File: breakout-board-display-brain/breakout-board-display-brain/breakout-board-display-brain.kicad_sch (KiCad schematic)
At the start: 8 parts, among them J1 Conn_01x15_Socket, J2 Conn_01x15_Socket, J3 Conn_01x16_Female, SW1 RotaryEncoder_Switch

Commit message: ...
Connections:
- net 0 renamed Pin_0
- net 1 renamed Pin_1
- net 10 renamed Pin_10
- net 18 renamed Pin_18
- net 19 renamed Pin_19
- net 2 renamed Pin_2
- net 3 renamed Pin_3
- net 4 renamed Pin_4
- net 5 renamed Pin_5
- net 6 renamed Pin_6
- net 7 renamed Pin_7
- net 8 renamed Pin_8
- net 9 renamed Pin_9
- no-connect marks 8 -> 14

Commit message: Amir approved: Rotary Encode Circuit
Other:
- note added: "Amir approved"
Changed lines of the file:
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@@
+    (effects (font (size 1.27 1.27)) (justify left bottom))
+  )
+  (text "Amir approved" (at 219.71 53.34 0)
     (effects (font (size 1.27 1.27)) (justify left bottom))
   )

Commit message: Update: nun approved!
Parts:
- removed R1, R2: 10k, symbol Device:R
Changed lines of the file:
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@@
     (comment 1 "erste Version")
   )
-  (junction (at 222.25 31.75) (diameter 0) (color 0 0 0 0)
-  )
   (junction (at 106.68 68.58) (diameter 0) (color 0 0 0 0)
   )
-  (junction (at 237.49 40.64) (diameter 0) (color 0 0 0 0)
-  )
   (junction (at 264.16 44.45) (diameter 0) (color 0 0 0 0)
   )
@@
   )
   (junction (at 106.68 50.8) (diameter 0) (color 0 0 0 0)
-  )
-  (junction (at 234.95 31.75) (diameter 0) (color 0 0 0 0)
   )
   (junction (at 49.53 55.88) (diameter 0) (color 0 0 0 0)
@@
     (stroke (width 0) (type default))
   )
-  (wire (pts (xy 234.95 31.75) (xy 238.76 31.75))
+  (wire (pts (xy 224.79 31.75) (xy 238.76 31.75))
     (stroke (width 0) (type default))
   )
@@
     (stroke (width 0) (type default))
   )
-  (wire (pts (xy 238.76 40.64) (xy 237.49 40.64))
+  (wire (pts (xy 238.76 40.64) (xy 224.79 40.64))
     (stroke (width 0) (type default))
   )
@@
     (stroke (width 0) (type default))
   )
-  (wire (pts (xy 222.25 22.86) (xy 222.25 31.75))
-    (stroke (width 0) (type default))
-  )
   (wire (pts (xy 116.84 49.53) (xy 123.19 49.53))
     (stroke (width 0) (type default))
@@
     (stroke (width 0) (type default))
   )
-  (wire (pts (xy 237.49 40.64) (xy 232.41 40.64))
-    (stroke (width 0) (type default))
-  )
   (wire (pts (xy 92.71 60.96) (xy 99.06 60.96))
     (stroke (width 0) (type default))
@@
     (stroke (width 0) (type default))
   )
-  (wire (pts (xy 222.25 31.75) (xy 222.25 40.64))
-    (stroke (width 0) (type default))
-  )
-  (wire (pts (xy 234.95 31.75) (xy 232.41 31.75))
-    (stroke (width 0) (type default))
-  )
   (wire (pts (xy 190.5 31.75) (xy 203.2 31.75))
     (stroke (width 0) (type default))
@@
     (stroke (width 0) (type default))
   )
-  (wire (pts (xy 237.49 29.21) (xy 237.49 40.64))
+  (wire (pts (xy 224.79 39.37) (xy 224.79 40.64))
     (stroke (width 0) (type default))
   )
@@
     (stroke (width 0) (type default))
   )
-  (wire (pts (xy 222.25 40.64) (xy 224.79 40.64))
-    (stroke (width 0) (type default))
-  )
   (wire (pts (xy 54.61 24.13) (xy 54.61 35.56))
     (stroke (width 0) (type default))
@@
     (stroke (width 0) (type default))
   )
-  (wire (pts (xy 222.25 31.75) (xy 224.79 31.75))
-    (stroke (width 0) (type default))
-  )
   (wire (pts (xy 63.5 40.64) (xy 68.58 40.64))
     (stroke (width 0) (type default))
@@
     (stroke (width 0) (type default))
   )
-  (wire (pts (xy 234.95 22.86) (xy 234.95 31.75))
-    (stroke (width 0) (type default))
-  )
   (polyline (pts (xy 215.9 15.24) (xy 215.9 76.2))
     (stroke (width 0) (type default))
@@
     (stroke (width 0) (type default))
   )
-  (text "CLK\n" (at 234.95 20.32 0)
+  (text "CLK\n" (at 224.79 36.83 0)
     (effects (font (size 1.27 1.27)) (justify left bottom))
   )
@@
     (effects (font (size 1.27 1.27)) (justify left bottom))
   )
-  (text "DT\n" (at 237.49 26.67 0)
+  (text "DT\n" (at 224.79 29.21 0)
     (effects (font (size 1.27 1.27)) (justify left bottom))
   )
@@
     (effects (font (size 1.27 1.27)) (justify left bottom))
   )
-  (label "Pin_4" (at 234.95 22.86 0) (fields_autoplaced)
+  (label "Pin_4" (at 224.79 31.75 0) (fields_autoplaced)
     (effects (font (size 1.27 1.27)) (justify left bottom))
   )
@@
     (effects (font (size 1.27 1.27)) (justify left bottom))
   )
-  (label "Pin_5" (at 237.49 29.21 0) (fields_autoplaced)
+  (label "Pin_5" (at 224.79 39.37 0) (fields_autoplaced)
     (effects (font (size 1.27 1.27)) (justify left bottom))
   )
@@
   )
   (label "Pin_19" (at 116.84 67.31 0) (fields_autoplaced)
-    (effects (font (size 1.27 1.27)) (justify left bottom))
-  )
-  (label "5V" (at 222.25 22.86 0) (fields_autoplaced)
     (effects (font (size 1.27 1.27)) (justify left bottom))
   )
@@
         )
       )
-    )
-  )
-  (symbol (lib_id "Device:R") (at 228.6 31.75 90) (unit 1)
-    (in_bom yes) (on_board yes) (dnp no) (fields_autoplaced)
-    (property "Reference" "R1" (at 228.6 26.67 90)
-      (effects (font (size 1.27 1.27)))
-    )
-    (property "Value" "10k" (at 228.6 29.21 90)
-      (effects (font (size 1.27 1.27)))
-    )
-    (property "Footprint" "" (at 228.6 33.528 90)
-      (effects (font (size 1.27 1.27)) hide)
-    )
-    (property "Datasheet" "~" (at 228.6 31.75 0)
-      (effects (font (size 1.27 1.27)) hide)
-    )
-    (pin "1")
-    (pin "2")
-    (instances
-      (project "breakout-board-display-brain"
-        (path "/860671aa-4c8a-4921-a8d3-0a28e74ec70f"
-          (reference "R1") (unit 1)
-        )
-      )
-    )
-  )
-  (symbol (lib_id "Device:R") (at 228.6 40.64 90) (unit 1)
-    (in_bom yes) (on_board yes) (dnp no) (fields_autoplaced)
-    (property "Reference" "R2" (at 228.6 35.56 90)
-      (effects (font (size 1.27 1.27)))
-    )
-    (property "Value" "10k" (at 228.6 38.1 90)
-      (effects (font (size 1.27 1.27)))
-    )
-    (property "Footprint" "" (at 228.6 42.418 90)
-      (effects (font (size 1.27 1.27)) hide)
-    )
-    (property "Datasheet" "~" (at 228.6 40.64 0)
-      (effects (font (size 1.27 1.27)) hide)
-    )
-    (pin "1")
-    (pin "2")
-    (instances
-      (project "breakout-board-display-brain"
-        (path "/860671aa-4c8a-4921-a8d3-0a28e74ec70f"
-          (reference "R2") (unit 1)
-        )
-      )

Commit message: further work on breakout board display brain
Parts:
- J1, J2: footprint (none) -> Connector_PinSocket_2.54mm:PinSocket_1x15_P2.54mm_Vertical
- SW1: footprint (none) -> Rotary_Encoder:RotaryEncoder_Alps_EC11E-Switch_Vertical_H20mm
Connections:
- net Pin_10: no longer DS1.12 (D5), J3.12 (Pin_12)
- net Pin_18: no longer DS1.13 (D6), J3.13 (Pin_13)
- net Pin_19: no longer DS1.14 (D7), J3.14 (Pin_14)
- net Pin_4: now also DS1.12 (D5), J3.12 (Pin_12); no longer SW1.A
- net Pin_5: now also DS1.13 (D6), J3.13 (Pin_13); no longer SW1.B
- net Pin_6: now also DS1.14 (D7), J3.14 (Pin_14); no longer SW1.S1
- net Pin_7: now also SW1.A
- net Pin_8: now also SW1.B
- net Pin_9: now also SW1.S1
- no-connect marks 14 -> 16
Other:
- note removed: "Amir approved"
- moved on the sheet: SW1

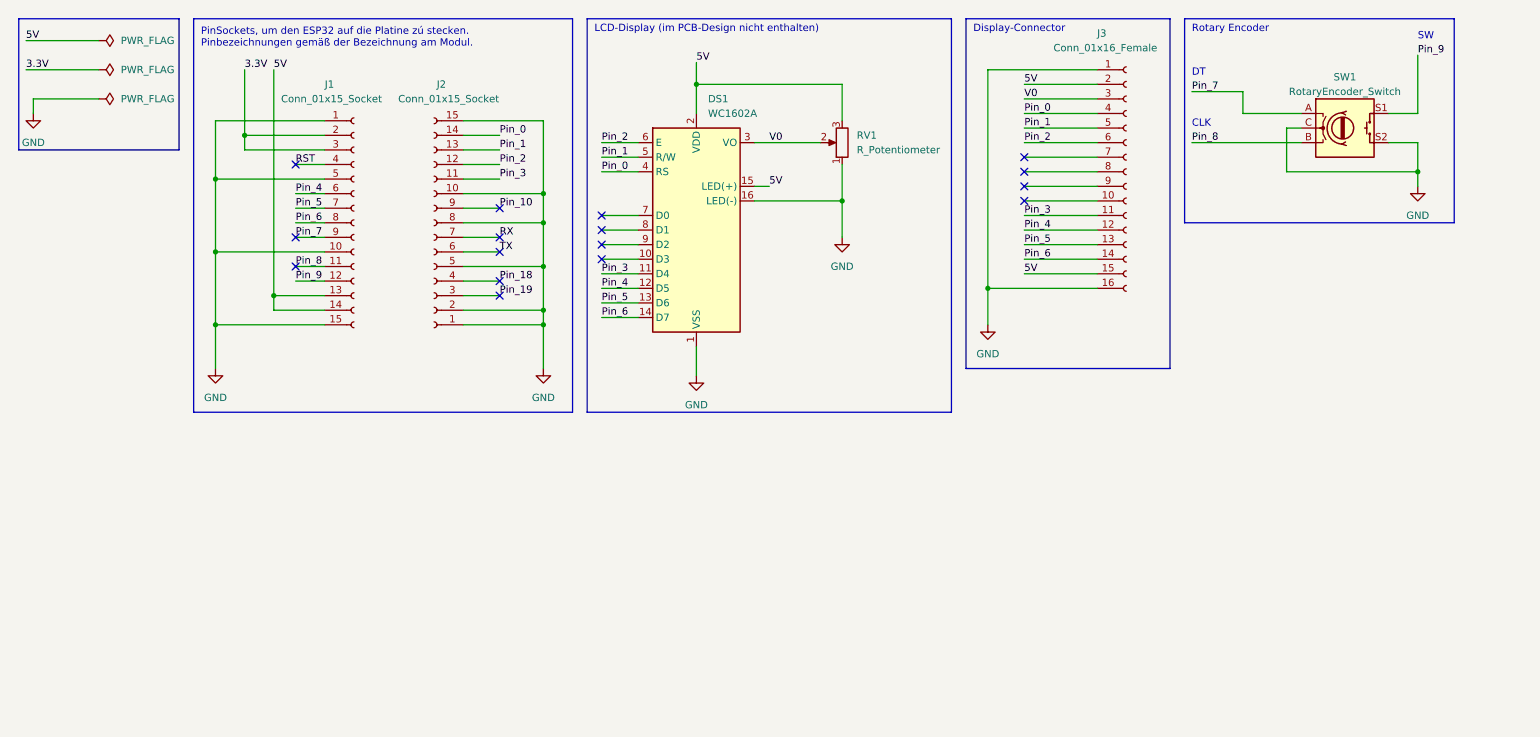
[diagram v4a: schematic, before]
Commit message: connector added to display-brain breakout board
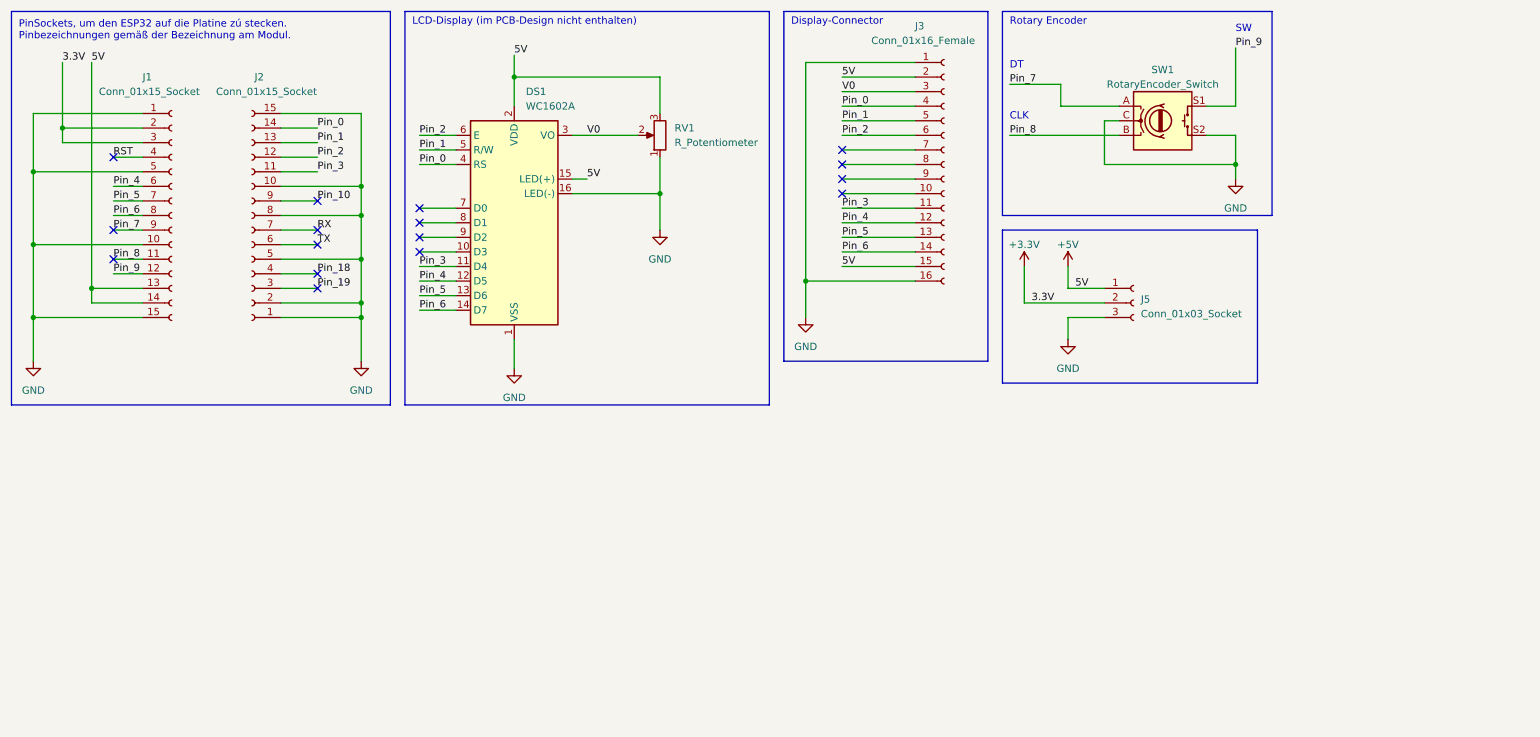
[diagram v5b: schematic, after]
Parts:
- added J5: Conn_01x03_Socket, Connector_PinSocket_2.54mm:PinSocket_1x03_P2.54mm_Vertical, symbol Connector:Conn_01x03_Socket
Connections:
- net GND: now also J5.3 (Pin_3)
- net 3.3V renamed +3.3V
- net +3.3V: now also J5.2 (Pin_2)
- net 5V renamed +5V
- net +5V: now also J5.1 (Pin_1)
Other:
- moved on the sheet: DS1, J1, J2, J3, RV1, SW1

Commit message: Routing
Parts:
- removed J5: Conn_01x03_Socket, Connector_PinSocket_2.54mm:PinSocket_1x03_P2.54mm_Vertical, symbol Connector:Conn_01x03_Socket
- added J4: Conn_01x02_Socket, Connector_PinSocket_2.54mm:PinSocket_1x02_P2.54mm_Vertical, symbol Connector:Conn_01x02_Socket
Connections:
- net +5V: now also J4.1 (Pin_1)
- net GND: now also J4.2 (Pin_2)
- net +3.3V renamed 3.3V
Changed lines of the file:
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@@
     (stroke (width 0) (type default))
   )
-  (wire (pts (xy 198.12 62.23) (xy 198.12 58.42))
+  (wire (pts (xy 190.5 62.23) (xy 190.5 58.42))
     (stroke (width 0) (type default))
   )
@@
     (stroke (width 0) (type default))
   )
-  (wire (pts (xy 198.12 67.31) (xy 204.47 67.31))
+  (wire (pts (xy 190.5 64.77) (xy 196.85 64.77))
     (stroke (width 0) (type default))
   )
@@
     (stroke (width 0) (type default))
   )
-  (wire (pts (xy 190.5 64.77) (xy 190.5 58.42))
-    (stroke (width 0) (type default))
-  )
   (wire (pts (xy 152.4 22.86) (xy 171.45 22.86))
     (stroke (width 0) (type default))
@@
     (stroke (width 0) (type default))
   )
-  (polyline (pts (xy 231.14 52.07) (xy 231.14 78.74))
+  (polyline (pts (xy 223.52 52.07) (xy 223.52 74.93))
     (stroke (width 0) (type default))
   )
@@
     (stroke (width 0) (type default))
   )
-  (wire (pts (xy 198.12 62.23) (xy 204.47 62.23))
+  (wire (pts (xy 190.5 62.23) (xy 196.85 62.23))
     (stroke (width 0) (type default))
   )
@@
     (stroke (width 0) (type default))
   )
-  (polyline (pts (xy 186.69 52.07) (xy 231.14 52.07))
+  (polyline (pts (xy 186.69 52.07) (xy 223.52 52.07))
     (stroke (width 0) (type default))
   )
@@
     (stroke (width 0) (type default))
   )
-  (wire (pts (xy 198.12 67.31) (xy 198.12 71.12))
+  (wire (pts (xy 190.5 64.77) (xy 190.5 68.58))
     (stroke (width 0) (type default))
   )
@@
     (stroke (width 0) (type default))
   )
-  (wire (pts (xy 190.5 64.77) (xy 204.47 64.77))
-    (stroke (width 0) (type default))
-  )
-  (polyline (pts (xy 231.14 78.74) (xy 186.69 78.74))
+  (polyline (pts (xy 223.52 74.93) (xy 186.69 74.93))
     (stroke (width 0) (type default))
   )
@@
     (stroke (width 0) (type default))
   )
-  (polyline (pts (xy 186.69 52.07) (xy 186.69 78.74))
+  (polyline (pts (xy 186.69 52.07) (xy 186.69 74.93))
     (stroke (width 0) (type default))
   )
@@
     (effects (font (size 1.27 1.27)) (justify left bottom))
   )
-  (label "5V" (at 199.39 62.23 0) (fields_autoplaced)
+  (label "5V" (at 191.77 62.23 0) (fields_autoplaced)
     (effects (font (size 1.27 1.27)) (justify left bottom))
   )
@@
   )
   (label "V0" (at 158.75 27.94 0) (fields_autoplaced)
-    (effects (font (size 1.27 1.27)) (justify left bottom))
-  )
-  (label "3.3V" (at 191.77 64.77 0) (fields_autoplaced)
     (effects (font (size 1.27 1.27)) (justify left bottom))
   )
@@
     )
   )
-  (symbol (lib_id "Connector:Conn_01x03_Socket") (at 209.55 64.77 0) (unit 1)
-    (in_bom yes) (on_board yes) (dnp no) (fields_autoplaced)
-    (property "Reference" "J5" (at 210.82 64.135 0)
-      (effects (font (size 1.27 1.27)) (justify left))
-    )
-    (property "Value" "Conn_01x03_Socket" (at 210.82 66.675 0)
-      (effects (font (size 1.27 1.27)) (justify left))
-    )
-    (property "Footprint" "Connector_PinSocket_2.54mm:PinSocket_1x03_P2.54mm_Vertical" (at 209.55 64.77 0)
-      (effects (font (size 1.27 1.27)) hide)
-    )
-    (property "Datasheet" "~" (at 209.55 64.77 0)
-      (effects (font (size 1.27 1.27)) hide)
-    )
-    (pin "1")
-    (pin "2")
-    (pin "3")
-    (instances
-      (project "breakout-board-display-brain"
-        (path "/860671aa-4c8a-4921-a8d3-0a28e74ec70f"
-          (reference "J5") (unit 1)
-        )
-      )
-    )
-  )
-  (symbol (lib_id "power:+3.3V") (at 190.5 58.42 0) (unit 1)
-    (in_bom yes) (on_board yes) (dnp no) (fields_autoplaced)
-    (property "Reference" "#PWR07" (at 190.5 62.23 0)
-      (effects (font (size 1.27 1.27)) hide)
-    )
-    (property "Value" "+3.3V" (at 190.5 54.61 0)
+  (symbol (lib_name "GND_1") (lib_id "power:GND") (at 74.93 74.93 0) (unit 1)
+    (in_bom yes) (on_board yes) (dnp no) (fields_autoplaced)
+    (property "Reference" "#PWR02" (at 74.93 81.28 0)
+      (effects (font (size 1.27 1.27)) hide)
+    )
+    (property "Value" "GND" (at 74.93 80.01 0)
+      (effects (font (size 1.27 1.27)))
+    )
+    (property "Footprint" "" (at 74.93 74.93 0)
+      (effects (font (size 1.27 1.27)) hide)
+    )
+    (property "Datasheet" "" (at 74.93 74.93 0)
+      (effects (font (size 1.27 1.27)) hide)
+    )
+    (pin "1")
+    (instances
+      (project "breakout-board-display-brain"
+        (path "/860671aa-4c8a-4921-a8d3-0a28e74ec70f"
+          (reference "#PWR02") (unit 1)
+        )
+      )
+    )
+  )
+  (symbol (lib_id "power:+5V") (at 190.5 58.42 0) (unit 1)
+    (in_bom yes) (on_board yes) (dnp no) (fields_autoplaced)
+    (property "Reference" "#PWR05" (at 190.5 62.23 0)
+      (effects (font (size 1.27 1.27)) hide)
+    )
+    (property "Value" "+5V" (at 190.5 54.61 0)
       (effects (font (size 1.27 1.27)))
     )
@@
     )
     (property "Datasheet" "" (at 190.5 58.42 0)
-      (effects (font (size 1.27 1.27)) hide)
-    )
-    (pin "1")
-    (instances
-      (project "breakout-board-display-brain"
-        (path "/860671aa-4c8a-4921-a8d3-0a28e74ec70f"
-          (reference "#PWR07") (unit 1)
-        )
-      )
-    )
-  )
-  (symbol (lib_name "GND_1") (lib_id "power:GND") (at 74.93 74.93 0) (unit 1)
-    (in_bom yes) (on_board yes) (dnp no) (fields_autoplaced)
-    (property "Reference" "#PWR02" (at 74.93 81.28 0)
-      (effects (font (size 1.27 1.27)) hide)
-    )
-    (property "Value" "GND" (at 74.93 80.01 0)
-      (effects (font (size 1.27 1.27)))
-    )
-    (property "Footprint" "" (at 74.93 74.93 0)
-      (effects (font (size 1.27 1.27)) hide)
-    )
-    (property "Datasheet" "" (at 74.93 74.93 0)
-      (effects (font (size 1.27 1.27)) hide)
-    )
-    (pin "1")
-    (instances
-      (project "breakout-board-display-brain"
-        (path "/860671aa-4c8a-4921-a8d3-0a28e74ec70f"
-          (reference "#PWR02") (unit 1)
-        )
-      )
-    )
-  )
-  (symbol (lib_id "power:+5V") (at 198.12 58.42 0) (unit 1)
-    (in_bom yes) (on_board yes) (dnp no) (fields_autoplaced)
-    (property "Reference" "#PWR05" (at 198.12 62.23 0)
-      (effects (font (size 1.27 1.27)) hide)
-    )
-    (property "Value" "+5V" (at 198.12 54.61 0)
-      (effects (font (size 1.27 1.27)))
-    )
-    (property "Footprint" "" (at 198.12 58.42 0)
-      (effects (font (size 1.27 1.27)) hide)
-    )
-    (property "Datasheet" "" (at 198.12 58.42 0)
       (effects (font (size 1.27 1.27)) hide)
     )
@@
     )
   )
-  (symbol (lib_name "GND_1") (lib_id "power:GND") (at 198.12 71.12 0) (unit 1)
-    (in_bom yes) (on_board yes) (dnp no) (fields_autoplaced)
-    (property "Reference" "#PWR06" (at 198.12 77.47 0)
-      (effects (font (size 1.27 1.27)) hide)
-    )
-    (property "Value" "GND" (at 198.12 76.2 0)
-      (effects (font (size 1.27 1.27)))
-    )
-    (property "Footprint" "" (at 198.12 71.12 0)
-      (effects (font (size 1.27 1.27)) hide)
-    )
-    (property "Datasheet" "" (at 198.12 71.12 0)
+  (symbol (lib_name "GND_1") (lib_id "power:GND") (at 190.5 68.58 0) (unit 1)
+    (in_bom yes) (on_board yes) (dnp no) (fields_autoplaced)
+    (property "Reference" "#PWR06" (at 190.5 74.93 0)
+      (effects (font (size 1.27 1.27)) hide)
+    )
+    (property "Value" "GND" (at 190.5 73.66 0)
+      (effects (font (size 1.27 1.27)))
+    )
+    (property "Footprint" "" (at 190.5 68.58 0)
+      (effects (font (size 1.27 1.27)) hide)
+    )
+    (property "Datasheet" "" (at 190.5 68.58 0)
       (effects (font (size 1.27 1.27)) hide)
     )
@@
         )
       )
+    )
+  )
+  (symbol (lib_id "Connector:Conn_01x02_Socket") (at 201.93 62.23 0) (unit 1)
+    (in_bom yes) (on_board yes) (dnp no) (fields_autoplaced)
+    (property "Reference" "J4" (at 203.2 62.865 0)
+      (effects (font (size 1.27 1.27)) (justify left))
+    )
+    (property "Value" "Conn_01x02_Socket" (at 203.2 65.405 0)
+      (effects (font (size 1.27 1.27)) (justify left))
+    )
+    (property "Footprint" "Connector_PinSocket_2.54mm:PinSocket_1x02_P2.54mm_Vertical" (at 201.93 62.23 0)
+      (effects (font (size 1.27 1.27)) hide)
+    )
+    (property "Datasheet" "~" (at 201.93 62.23 0)
+      (effects (font (size 1.27 1.27)) hide)
+    )
+    (pin "1")
+    (pin "2")
+    (instances
+      (project "breakout-board-display-brain"
+        (path "/860671aa-4c8a-4921-a8d3-0a28e74ec70f"
+          (reference "J4") (unit 1)
+        )
+      )

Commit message: ...
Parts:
- removed J1, J2: Conn_01x15_Socket, Connector_PinSocket_2.54mm:PinSocket_1x15_P2.54mm_Vertical, symbol Connector:Conn_01x15_Socket
- added J1, J2: Conn_01x19_Socket, Connector_PinSocket_2.54mm:PinSocket_1x19_P2.54mm_Vertical, symbol Connector:Conn_01x19_Socket
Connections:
- net GND: now also J1.14 (Pin_14), J2.13 (Pin_13), J2.19 (Pin_19)
- net +5V renamed 5V
- net 5V: now also J1.19 (Pin_19)
- net Pin_0 renamed IO0
- net IO0: now also J2.6 (Pin_6)
- net Pin_1 renamed IO1
- net Pin_2 renamed IO2
- net IO2: now also J2.5 (Pin_5)
- net Pin_3 renamed IO3
- net Pin_4 renamed IO4
- net IO4: now also J2.7 (Pin_7)
- net Pin_5 renamed IO5
- net IO5: now also J2.10 (Pin_10)
- net Pin_6 renamed IO6
- net Pin_7 renamed IO7
- net Pin_8 renamed IO8
- net Pin_9 renamed IO9
- new net 3V3: J1.1 (Pin_1)
- new net CLK: J2.1 (Pin_1)
- new net CMD: J1.18 (Pin_18)
- new net EN: J1.2 (Pin_2)
- new net IO12: J1.13 (Pin_13)
- new net IO13: J1.15 (Pin_15)
- new net IO14: J1.12 (Pin_12)
- new net IO15: J2.4 (Pin_4)
- new net IO16: J2.8 (Pin_8)
- new net IO17: J2.9 (Pin_9)
- new net IO18: J2.11 (Pin_11)
- new net IO19: J2.12 (Pin_12)
- new net IO21: J2.14 (Pin_14)
- new net IO22: J2.17 (Pin_17)
- new net IO23: J2.18 (Pin_18)
- new net IO25: J1.9 (Pin_9)
- new net IO26: J1.10 (Pin_10)
- new net IO27: J1.11 (Pin_11)
- new net IO32: J1.7 (Pin_7)
- new net IO33: J1.8 (Pin_8)
- new net IO34: J1.5 (Pin_5)
- new net IO35: J1.6 (Pin_6)
- new net RXD0: J2.15 (Pin_15)
- new net SD0: J2.2 (Pin_2)
- new net SD1: J2.3 (Pin_3)
- new net SD2: J1.16 (Pin_16)
- new net SD3: J1.17 (Pin_17)
- new net SENSOR_VN: J1.4 (Pin_4)
- new net SENSOR_VP: J1.3 (Pin_3)
- new net TXD0: J2.16 (Pin_16)
- no-connect marks 16 -> 8
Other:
- moved on the sheet: DS1, J3, J4, RV1, SW1
